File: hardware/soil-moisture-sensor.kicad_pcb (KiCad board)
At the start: 2 copper layers, 185.3 x 23 mm, 8 parts

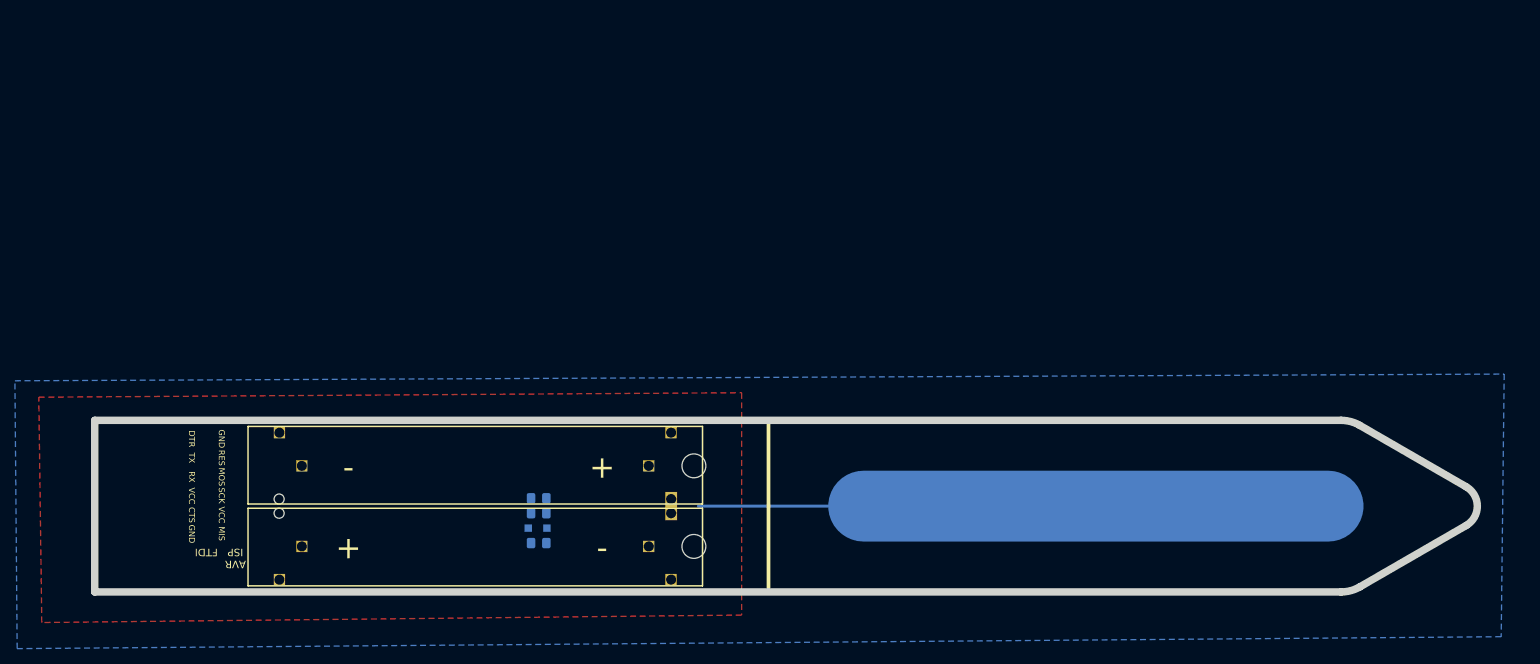
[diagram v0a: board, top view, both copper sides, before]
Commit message: changed power structure - removed ldo
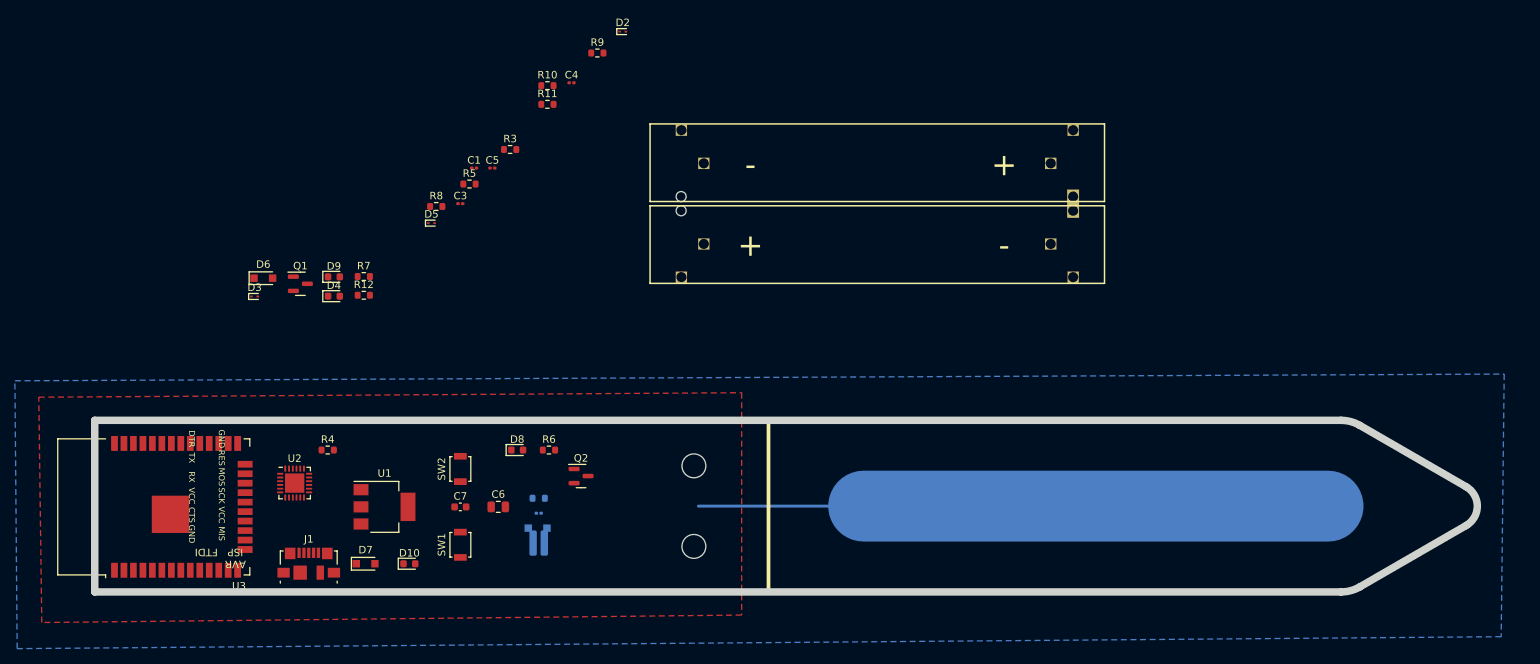
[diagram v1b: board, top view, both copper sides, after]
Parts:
- added C1: 0.1uF, Capacitor_SMD:C_0201_0603Metric, F.Cu at (116.1, 68.9)
- added C3: 22uF, Capacitor_SMD:C_0201_0603Metric, F.Cu at (114.3, 73.7)
- added C4: 0.1uF, Capacitor_SMD:C_0201_0603Metric, F.Cu at (129.2, 57.5)
- added C5: 4.7uF, Capacitor_SMD:C_0201_0603Metric, F.Cu at (118.6, 68.9)
- added C6: 22uF, Capacitor_SMD:C_0805_2012Metric, F.Cu at (119.4, 114.3)
- added C7: 0.1uF, Capacitor_SMD:C_0603_1608Metric, F.Cu at (114.3, 114.3)
- added D10: RX_LED, LED_SMD:LED_0603_1608Metric, F.Cu at (107.5, 121.9)
- added D2: ESD9B3.3ST5G, Diode_SMD:D_SOD-923, F.Cu at (136.1, 50.6)
- added D3: ESD9B3.3ST5G, Diode_SMD:D_SOD-923, F.Cu at (86.7, 86.1)
- added D4: D_Schottky, Diode_SMD:D_0603_1608Metric, F.Cu at (97.3, 86.1)
- added D5: ESD9B3.3ST5G, Diode_SMD:D_SOD-923, F.Cu at (110.4, 76.3)
- added D6: D_Schottky, Diode_SMD:D_SOD-323_HandSoldering, F.Cu at (87.9, 83.7)
- added D7: D_Schottky, Diode_SMD:D_SOD-323_HandSoldering, F.Cu at (101.6, 121.9)
- added D8: RED_LED, LED_SMD:LED_0603_1608Metric, F.Cu at (121.9, 106.7)
- added D9: TX_LED, LED_SMD:LED_0603_1608Metric, F.Cu at (97.3, 83.5)
- added J1: USB_B_Micro, Connector_USB:USB_Micro-B_Molex_47346-0001, F.Cu at (94.0, 121.9)
- added Q1: Q_NPN_BEC, Package_TO_SOT_SMD:SOT-23, F.Cu at (92.9, 84.4)
- added Q2: Q_NPN_BEC, Package_TO_SOT_SMD:SOT-23, F.Cu at (130.5, 110.2)
- added R10: 10k, Resistor_SMD:R_0603_1608Metric, F.Cu at (126.0, 57.8)
- added R11: 2k, Resistor_SMD:R_0603_1608Metric, F.Cu at (126.0, 60.4)
- added R12: 2k, Resistor_SMD:R_0603_1608Metric, F.Cu at (101.4, 85.9)
- added R3: 10k, Resistor_SMD:R_0603_1608Metric, F.Cu at (121.0, 66.4)
- added R4: 10k, Resistor_SMD:R_0603_1608Metric, F.Cu at (96.5, 106.7)
- added R5: 2k, Resistor_SMD:R_0603_1608Metric, F.Cu at (115.5, 71.0)
- added R6: 22.1k, Resistor_SMD:R_0603_1608Metric, F.Cu at (126.2, 106.7)
- added R7: 47.5k, Resistor_SMD:R_0603_1608Metric, F.Cu at (101.4, 83.4)
- added R8: 2k, Resistor_SMD:R_0603_1608Metric, F.Cu at (111.1, 74.0)
- added R9: 10k, Resistor_SMD:R_0603_1608Metric, F.Cu at (132.7, 53.5)
- added SW1: SW_Push, Button_Switch_SMD:SW_SPST_B3U-1000P, F.Cu at (114.3, 119.4)
- added SW2: SW_Push, Button_Switch_SMD:SW_SPST_B3U-1000P, F.Cu at (114.3, 109.2)
- added U1: AMS1117-3.3, Package_TO_SOT_SMD:SOT-223-3_TabPin2, F.Cu at (104.1, 114.3)
- added U2: CP2102N-Axx-xQFN24, Package_DFN_QFN:QFN-24-1EP_4x4mm_P0.5mm_EP2.6x2.6mm, F.Cu at (92.1, 111.1)
- added U3: ESP32-WROOM-32D, RF_Module:ESP32-WROOM-32, F.Cu at (76.2, 114.3)
- C2: footprint Capacitor_SMD:C_0805_2012Metric_Pad1.15x1.40mm_HandSolder -> Capacitor_SMD:C_0201_0603Metric
- R1: footprint Resistor_SMD:R_0805_2012Metric_Pad1.15x1.40mm_HandSolder -> Resistor_SMD:R_0612_1632Metric
- R2: footprint Resistor_SMD:R_0805_2012Metric_Pad1.15x1.40mm_HandSolder -> Resistor_SMD:R_0603_1608Metric
- moved BT1 67.4 mm to (170.2, 73.7)
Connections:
- net SENSOR-OUT renamed /SENSOR_OUT
- R1 pad 2: SENSOR-IN -> /SENSOR_IN

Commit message: placement pretty much done
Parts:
- removed C3: 22uF, Capacitor_SMD:C_0201_0603Metric
- removed D4: D_Schottky, Diode_SMD:D_0603_1608Metric
- removed D7: D_Schottky, Diode_SMD:D_SOD-323_HandSoldering
- removed U1: AMS1117-3.3, Package_TO_SOT_SMD:SOT-223-3_TabPin2
- BT1: footprint MyFootprints:BatteryHolder_Keystone_597_591_2AAA_3V -> kicad_footprints:CR123A Battery Holder; moved to B.Cu
- C2, D1, R2: moved to F.Cu
- R1: footprint Resistor_SMD:R_0612_1632Metric -> Resistor_SMD:R_0603_1608Metric; moved to F.Cu
- moved D2 79.3 mm to (94.2, 117.9), turned to 90 degrees
- moved R9 74.9 mm to (103.9, 122.6)
- moved BT1 67.7 mm to (116.0, 114.2), turned to 0 degrees
- moved R10 60.4 mm to (95.6, 110.0), turned to 90 degrees
- moved C4 60.2 mm to (99.7, 109.9), turned to -90 degrees
- moved R11 58.1 mm to (91.5, 107.1), turned to 180 degrees
- moved C5 53.9 mm to (86.8, 112.4), turned to 180 degrees
- moved R3 49.7 mm to (97.1, 110.0), turned to -90 degrees
- moved R8 48.5 mm to (91.7, 118.5)
- moved D5 47.5 mm to (88.5, 118.4), turned to 90 degrees
- moved R5 41.6 mm to (94.7, 107.1)
- moved Q2 41.5 mm to (89.0, 110.0)
- moved C1 39.8 mm to (103.4, 106.6)
- moved C2 38.2 mm to (86.7, 118.5), turned to -90 degrees
- moved R2 38.0 mm to (86.8, 114.6), turned to 90 degrees
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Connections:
- C6 pad 1: GND -> +BATT
- C7 pad 1: GND -> +BATT
- D2 pad 2: /USB_5V -> +5V
- J1 pad 1: /USB_5V -> +5V
- R10 pad 2: unconnected-(R10-Pad2) -> GND
- R6 pad 1: /USB_5V -> +5V
- R9 pad 1: +3V3 -> +BATT
- U2 pad 5: +3V3 -> Net-(U2-Pad5)
- U2 pad 6: +3V3 -> Net-(U2-Pad5)
- U2 pad 7: unconnected-(U2-Pad7) -> +5V
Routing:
- removed copper zone on F.Cu, net GND
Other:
- copper layers 2 -> 4
- board text added: "BAT"
- board text added: "BOOT LOADER"
- board text added: "RST"

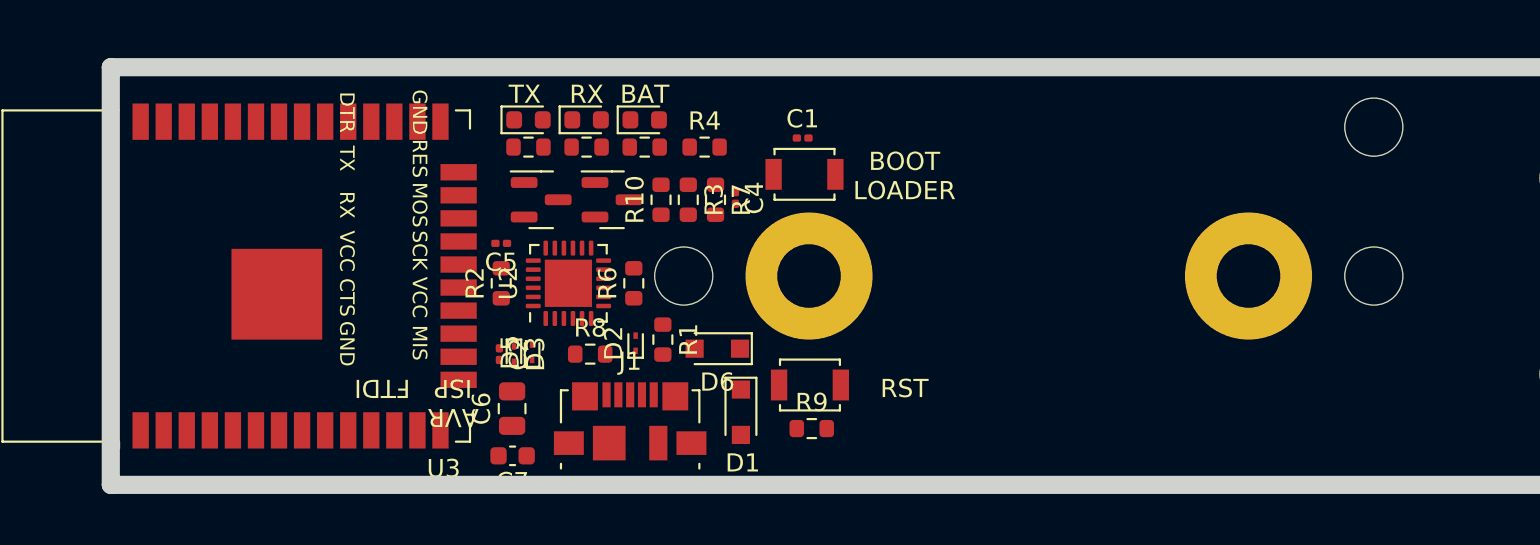
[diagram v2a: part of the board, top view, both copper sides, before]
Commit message: updated cr123a fp
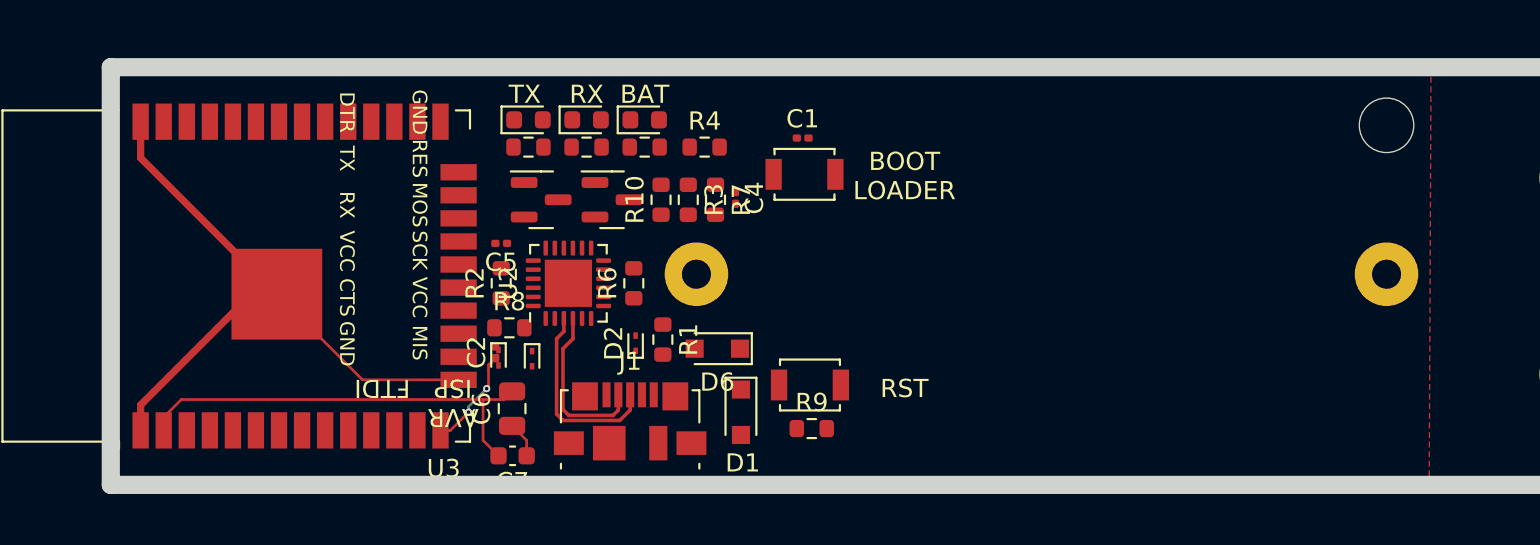
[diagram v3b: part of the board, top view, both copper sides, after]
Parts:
- moved R8 4.68 mm to (87.2, 117.0)
- moved D5 1.87 mm to (86.7, 118.7), turned to -90 degrees
- moved D3 1.03 mm to (88.5, 118.8)
- moved BT1 0.71 mm to (116.7, 114.1)
- moved C2 0.22 mm to (86.5, 118.4), turned to 90 degrees
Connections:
- net /USB_DM renamed /USB_N
- net /USB_DP renamed /USB_P
- R5 pad 1: +3V3 -> +BATT
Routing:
- net GND: track 0.00 -> 36.0 mm
- net Net-(C6-Pad2): track 0.00 -> 24.0 mm
- net /USB_P: track 0.00 -> 10.7 mm
- net /USB_N: track 0.00 -> 9.39 mm
- net /SENSOR_OUT: track 0.00 -> 5.57 mm, vias 0 -> 2
- net +BATT: track 0.00 -> 1.98 mm
- added copper zone on F.Cu, net GND

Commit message: layout finished
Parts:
- removed D1: D_Schottky, Diode_SMD:D_SOD-323_HandSoldering
- moved R9 21.4 mm to (86.8, 109.8), turned to -90 degrees
- moved SW2 10.7 mm to (103.1, 109.5)
- moved R4 7.60 mm to (97.2, 114.7), turned to 90 degrees
- moved R1 6.10 mm to (99.7, 122.3), turned to 90 degrees
- moved R7 5.51 mm to (95.6, 114.6), turned to 90 degrees
- moved D6 4.54 mm to (101.4, 121.8), turned to -90 degrees
- moved D5 4.02 mm to (90.7, 119.1), turned to 180 degrees
- moved C4 3.77 mm to (103.1, 111.6), turned to 180 degrees
- moved SW1 3.15 mm to (103.1, 105.5)
- moved R10 2.74 mm to (98.3, 110.0)
- moved R3 2.74 mm to (99.8, 110.0)
- moved BT1 2.74 mm to (119.4, 114.1)
- moved Q1 2.74 mm to (95.6, 110.0)
- moved Q2 2.74 mm to (91.7, 110.0)
- moved D2 1.75 mm to (92.7, 118.8), turned to -90 degrees
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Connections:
- D10 pad 2: +3V3 -> Net-(U2-Pad5)
- D9 pad 2: +3V3 -> Net-(U2-Pad5)
- R8 pad 1: +3V3 -> Net-(U2-Pad5)
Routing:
- net /EN: track 0.00 -> 63.8 mm, vias 0 -> 6
- net /Sensor_Track: track 53.3 -> 103.7 mm, vias 0 -> 1
- net /SENSOR_IN: track 0.00 -> 31.1 mm, vias 0 -> 2
- net Net-(U2-Pad5): track 0.00 -> 27.9 mm, vias 0 -> 4
- net /IO0: track 0.00 -> 27.2 mm
- net /SENSOR_OUT: track 5.57 -> 29.4 mm, vias 2 -> 4
- net /TXD: track 0.00 -> 23.3 mm, vias 0 -> 3
- net /RXD: track 0.00 -> 21.4 mm, vias 0 -> 2
- net /DTR: track 0.00 -> 18.4 mm, vias 0 -> 2
- net Net-(Q2-Pad1): track 0.00 -> 16.5 mm, vias 0 -> 2
- net /RTS: track 0.00 -> 14.5 mm, vias 0 -> 2
- net Net-(R11-Pad1): track 0.00 -> 13.1 mm, vias 0 -> 2
- net GND: track 36.0 -> 48.7 mm, vias 0 -> 10
- net Net-(R12-Pad1): track 0.00 -> 10.4 mm, vias 0 -> 2
- net +5V: track 0.00 -> 9.92 mm
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- added copper zone on In2.Cu, net +BATT
- added copper zone on In1.Cu, net GND

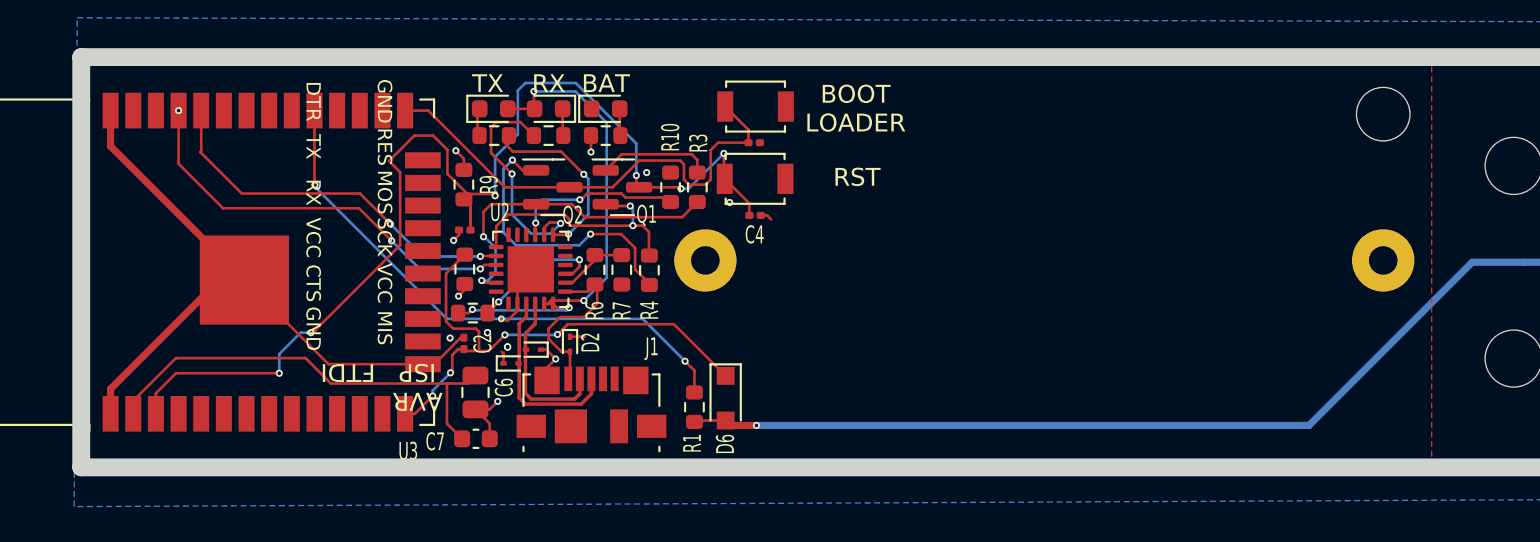
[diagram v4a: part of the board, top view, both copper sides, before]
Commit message: removed esd diodes, changed sensor out to adc pin
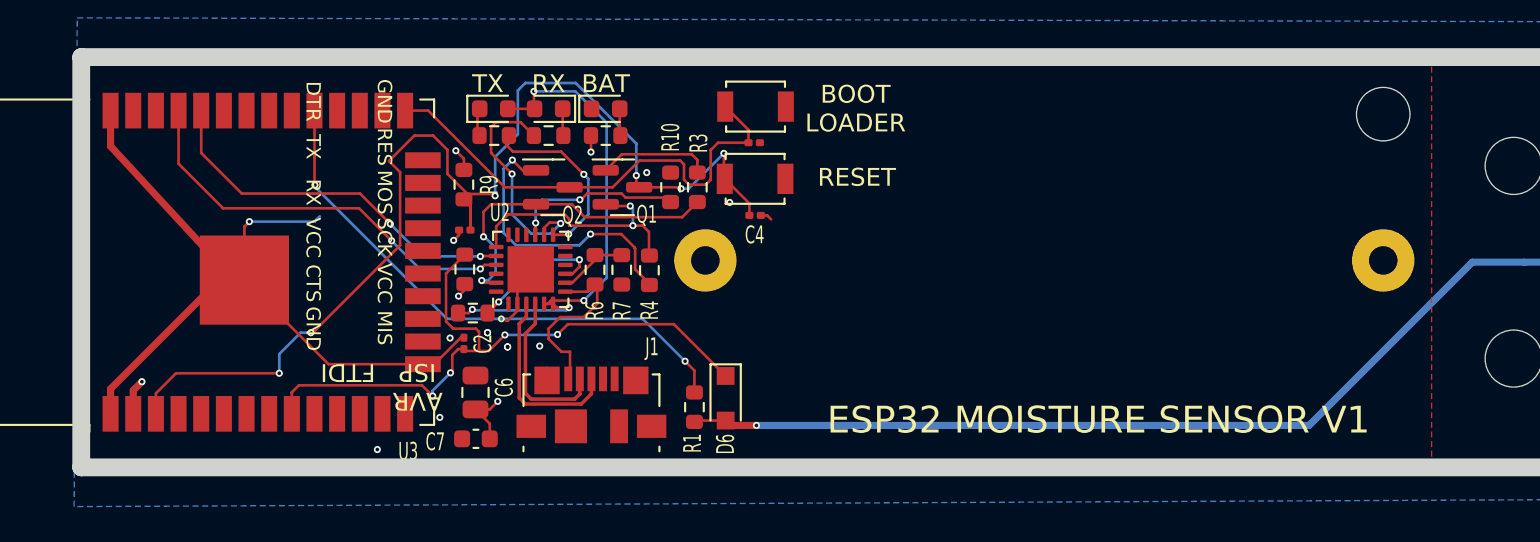
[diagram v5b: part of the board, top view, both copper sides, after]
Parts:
- removed D2, D3, D5: ESD9B3.3ST5G, Diode_SMD:D_SOD-923
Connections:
- C6 pad 2: Net-(C6-Pad2) -> GND
- C7 pad 2: Net-(C6-Pad2) -> GND
- U3 pad 14: /SENSOR_OUT -> unconnected-(U3-Pad14)
- U3 pad 2: Net-(C6-Pad2) -> +BATT
- U3 pad 9: unconnected-(U3-Pad9) -> /SENSOR_OUT
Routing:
- net Net-(C6-Pad2): track 25.2 -> 0.00 mm
- net +BATT: track 5.64 -> 23.1 mm, vias 3 -> 4
- net /SENSOR_OUT: track 29.4 -> 36.9 mm
- net GND: track 48.7 -> 53.3 mm, vias 10 -> 13
- net /TXD: vias 3 -> 2
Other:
- board text added: "ESP32 MOISTURE SENSOR V1"
- board text added: "RESET"
- board text removed: "RST"

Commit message: re-did a load of routing
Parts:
- added C3: 4.7uF, Capacitor_SMD:C_0603_1608Metric, F.Cu at (87.4, 121.0)
- C1, C2, C4, C5: footprint Capacitor_SMD:C_0201_0603Metric -> Capacitor_SMD:C_0603_1608Metric
- C6: value 22uF -> 4.7uF; footprint Capacitor_SMD:C_0805_2012Metric -> Capacitor_SMD:C_0603_1608Metric
- moved C4 2.05 mm to (104.5, 113.0)
- moved R8 2.02 mm to (88.3, 118.8), turned to 90 degrees
- moved SW2 1.58 mm to (104.3, 110.5)
- moved C1 1.42 mm to (104.4, 107.8)
- moved SW1 1.27 mm to (104.3, 105.2)
- moved C6 1.10 mm to (87.4, 122.6), turned to 180 degrees
- moved R2 1.05 mm to (86.7, 115.7)
- moved R9 0.30 mm to (86.7, 109.5)
- moved C5 0.22 mm to (86.7, 112.6), turned to -90 degrees
- moved C7 0.20 mm to (87.4, 124.3)
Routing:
- net GND: track 53.3 -> 89.0 mm, vias 13 -> 14
- net /SENSOR_OUT: track 36.9 -> 33.0 mm, vias 4 -> 3
- net /IO0: track 27.2 -> 28.9 mm
- net +BATT: track 23.1 -> 24.4 mm
- net Net-(R8-Pad2): track 7.74 -> 8.56 mm
- net /EN: track 63.8 -> 63.1 mm
- net Net-(D10-Pad2): track 27.9 -> 28.3 mm, vias 4 -> 3
- removed copper zone on F.Cu, net GND

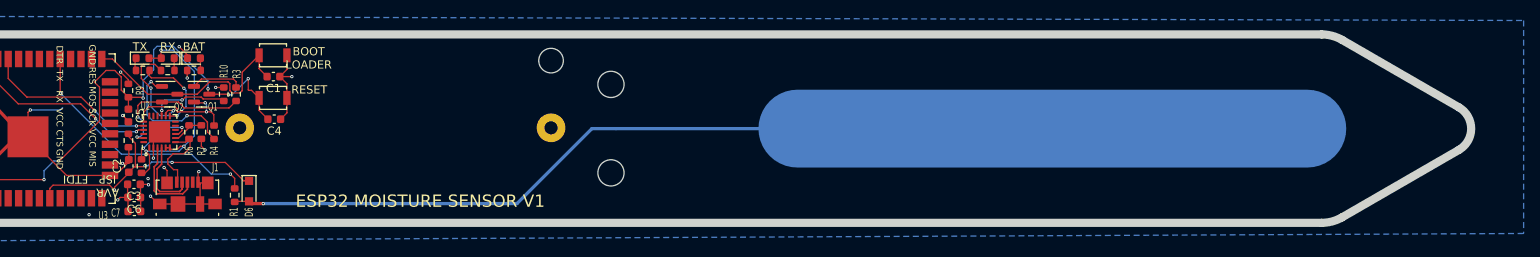
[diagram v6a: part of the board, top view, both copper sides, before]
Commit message: added bat mon circuit, made bat led a user led
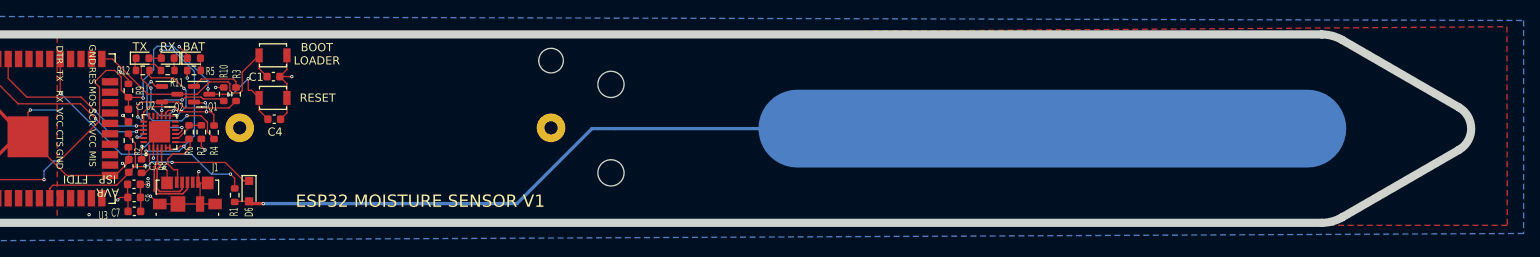
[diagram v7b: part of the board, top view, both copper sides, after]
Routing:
- net /SENSOR_OUT: track 33.0 -> 32.3 mm, vias 3 -> 2
- added copper zone on F.Cu, net GND
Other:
- rule pad_to_mask_clearance: 0.075 -> 0

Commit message: FIXED SOME DRC ERRORS
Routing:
- net +BATT: track 24.4 -> 24.9 mm
- net /EN: track 63.1 -> 62.5 mm
